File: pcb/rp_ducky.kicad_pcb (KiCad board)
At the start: 4 copper layers, 14 x 30 mm, 31 parts, among them J1 USB_A, SW1 R-667799, SW2 R-667799, U1 TCR2EE33, U2 W25Q32JVZP, U3 RP2040, Y1 Crystal_GND24

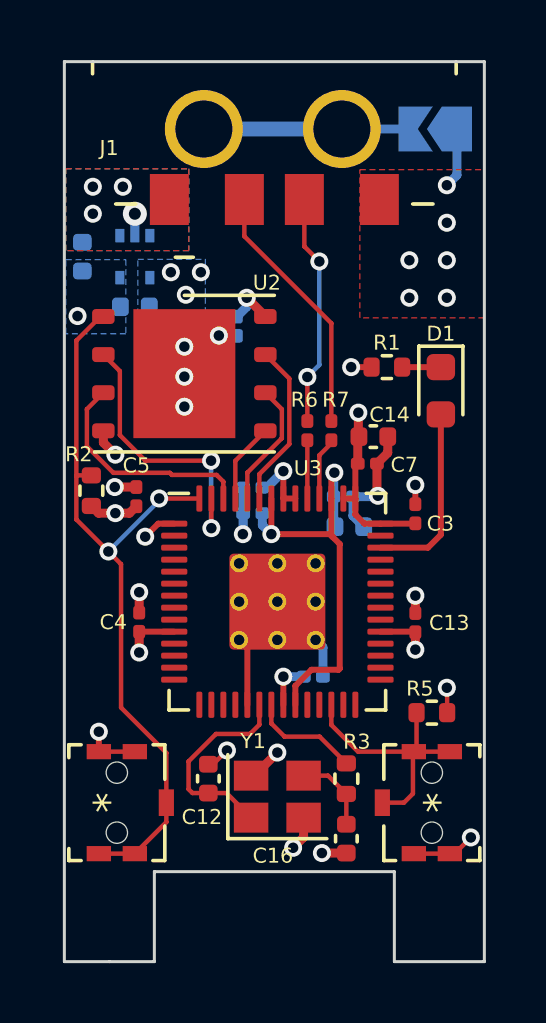
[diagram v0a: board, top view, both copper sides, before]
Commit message: use 0402 parts only, on the bottom use larger solderable pads
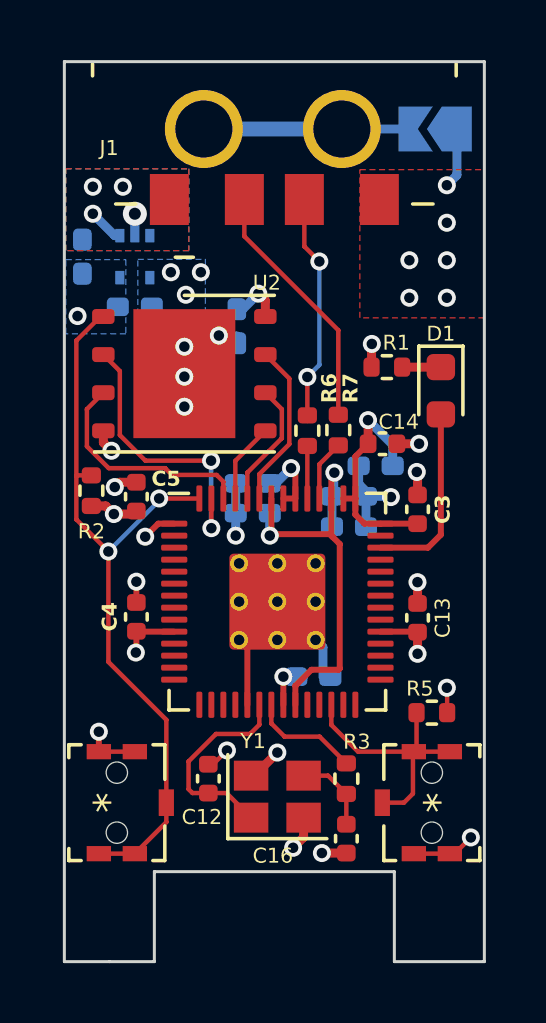
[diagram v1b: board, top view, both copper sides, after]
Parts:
- C1, C2, C6: footprint Capacitor_SMD:C_0402_1005Metric -> Capacitor_SMD:C_0402_1005Metric_Pad0.74x0.62mm_HandSolder
- C10, C11, C15, C8, C9: footprint Capacitor_SMD:C_0201_0603Metric -> Capacitor_SMD:C_0402_1005Metric_Pad0.74x0.62mm_HandSolder
- C13, C3, C4, C5: footprint Capacitor_SMD:C_0201_0603Metric -> Capacitor_SMD:C_0402_1005Metric
- C7: footprint Capacitor_SMD:C_0201_0603Metric -> Capacitor_SMD:C_0402_1005Metric_Pad0.74x0.62mm_HandSolder; moved to B.Cu
- R6, R7: footprint Resistor_SMD:R_0201_0603Metric -> Resistor_SMD:R_0402_1005Metric
- moved C14 0.39 mm to (90.6, 52.7)
- moved C7 0.29 mm to (90.4, 53.5), turned to 0 degrees
- moved R7 0.23 mm to (89.1, 52.3)
- moved C4 0.20 mm to (82.4, 58.5)
- moved C9 0.19 mm to (89.5, 54.5)
- moved C13 0.18 mm to (91.8, 58.5)
- moved C3 0.17 mm to (91.8, 54.9)
- moved C15 0.14 mm to (86.3, 54.1)
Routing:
- net +3V3: track 18.7 -> 20.7 mm
- net GND: track 26.4 -> 24.5 mm, vias 26 -> 27
- net +5V: track 0.00 -> 1.20 mm
- net +1V1: track 16.8 -> 15.8 mm
